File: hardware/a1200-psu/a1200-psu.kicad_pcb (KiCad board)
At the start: 2 copper layers, 147 x 76 mm, 28 parts, among them Q1 P2N60, U1 UC3844_DIP8, U2 PC817, U3 TL431D

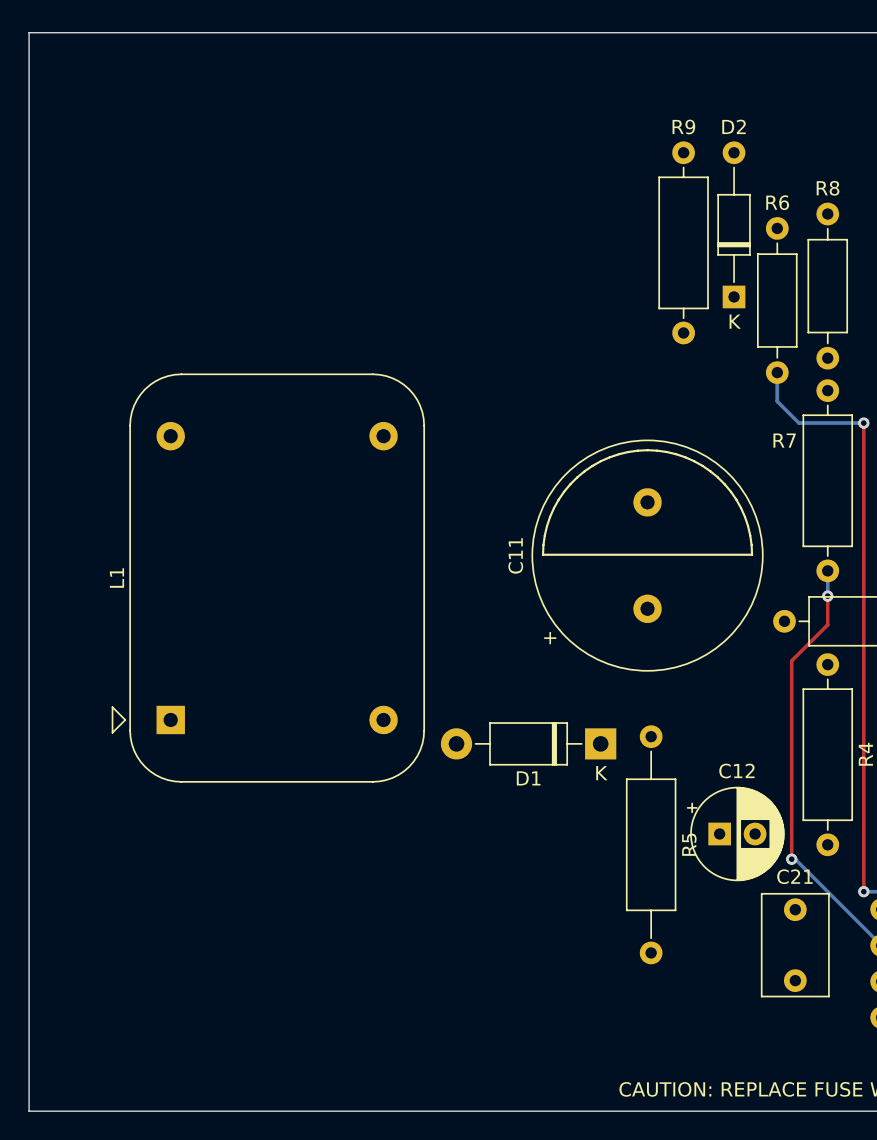
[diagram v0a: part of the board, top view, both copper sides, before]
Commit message: Add more components to PCB
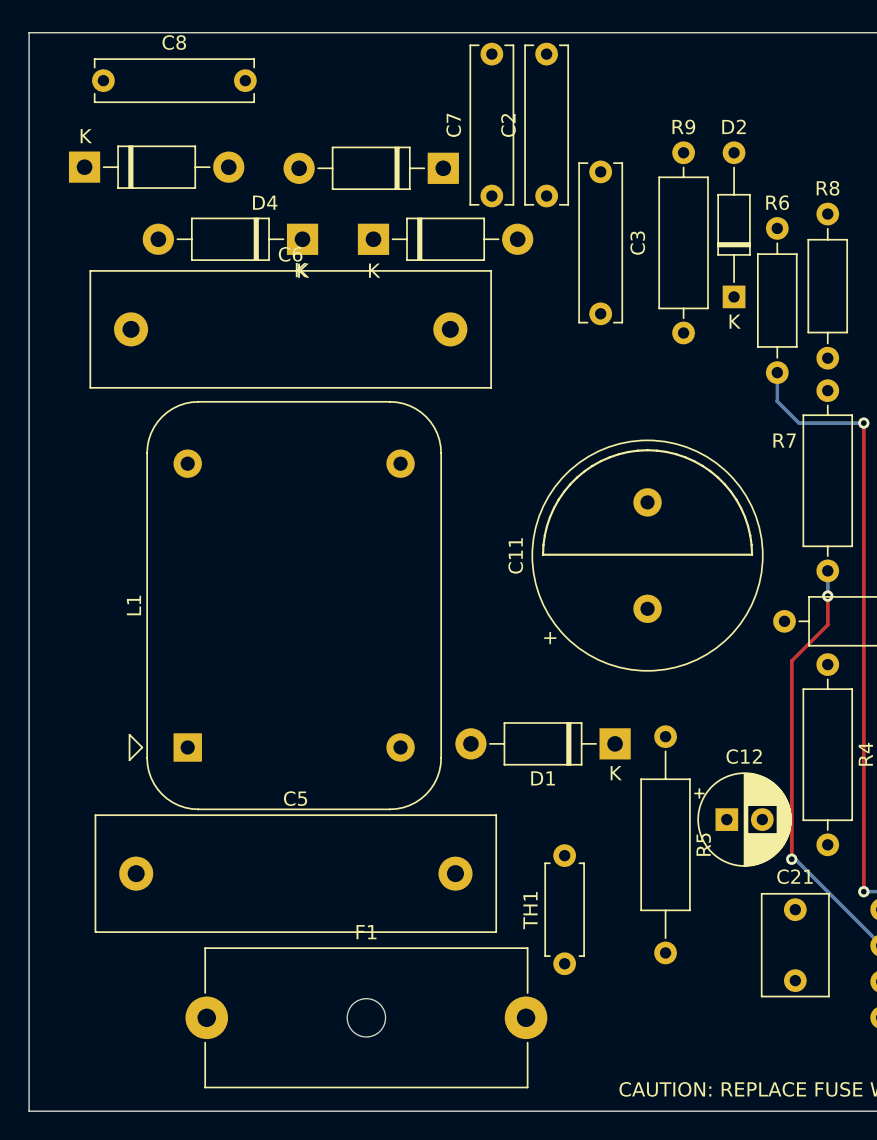
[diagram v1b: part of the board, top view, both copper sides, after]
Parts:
- added C2: 4n7, Capacitor_THT:C_Rect_L11.0mm_W2.8mm_P10.00mm_MKT, F.Cu at (109.2, 64.0)
- added C3: 4n7, Capacitor_THT:C_Rect_L11.0mm_W2.8mm_P10.00mm_MKT, F.Cu at (113.0, 62.3)
- added C5: 220nF, Capacitor_THT:C_Rect_L28.0mm_W8.0mm_P22.50mm_MKS4, F.Cu at (80.3, 111.8)
- added C6: 220nF, Capacitor_THT:C_Rect_L28.0mm_W8.0mm_P22.50mm_MKS4, F.Cu at (79.9, 73.4)
- added C7: 4n7, Capacitor_THT:C_Rect_L11.0mm_W2.8mm_P10.00mm_MKT, F.Cu at (105.4, 64.0)
- added C8: 4n7, Capacitor_THT:C_Rect_L11.0mm_W2.8mm_P10.00mm_MKT, F.Cu at (78.0, 55.9)
- added D4: 1N4007, Amiga 1200:Diode_Bridge, F.Cu at (89.4, 64.5)
- added F1: 250V T 1A, Fuse:Fuseholder_Cylinder-5x20mm_Schurter_0031_8201_Horizontal_Open, F.Cu at (85.3, 121.9)
- added TH1: 30R, Resistor_THT:R_Axial_DIN0207_L6.3mm_D2.5mm_P7.62mm_Horizontal, F.Cu at (110.5, 118.1)
- moved L1 2.28 mm to (83.9, 102.9)
- moved C12 1.14 mm to (121.9, 108.0)
- moved D1 1.02 mm to (114.0, 102.6)
- moved R5 1.02 mm to (117.6, 102.1)
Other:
- board text removed: "TODO: Change footprint to 22mm"

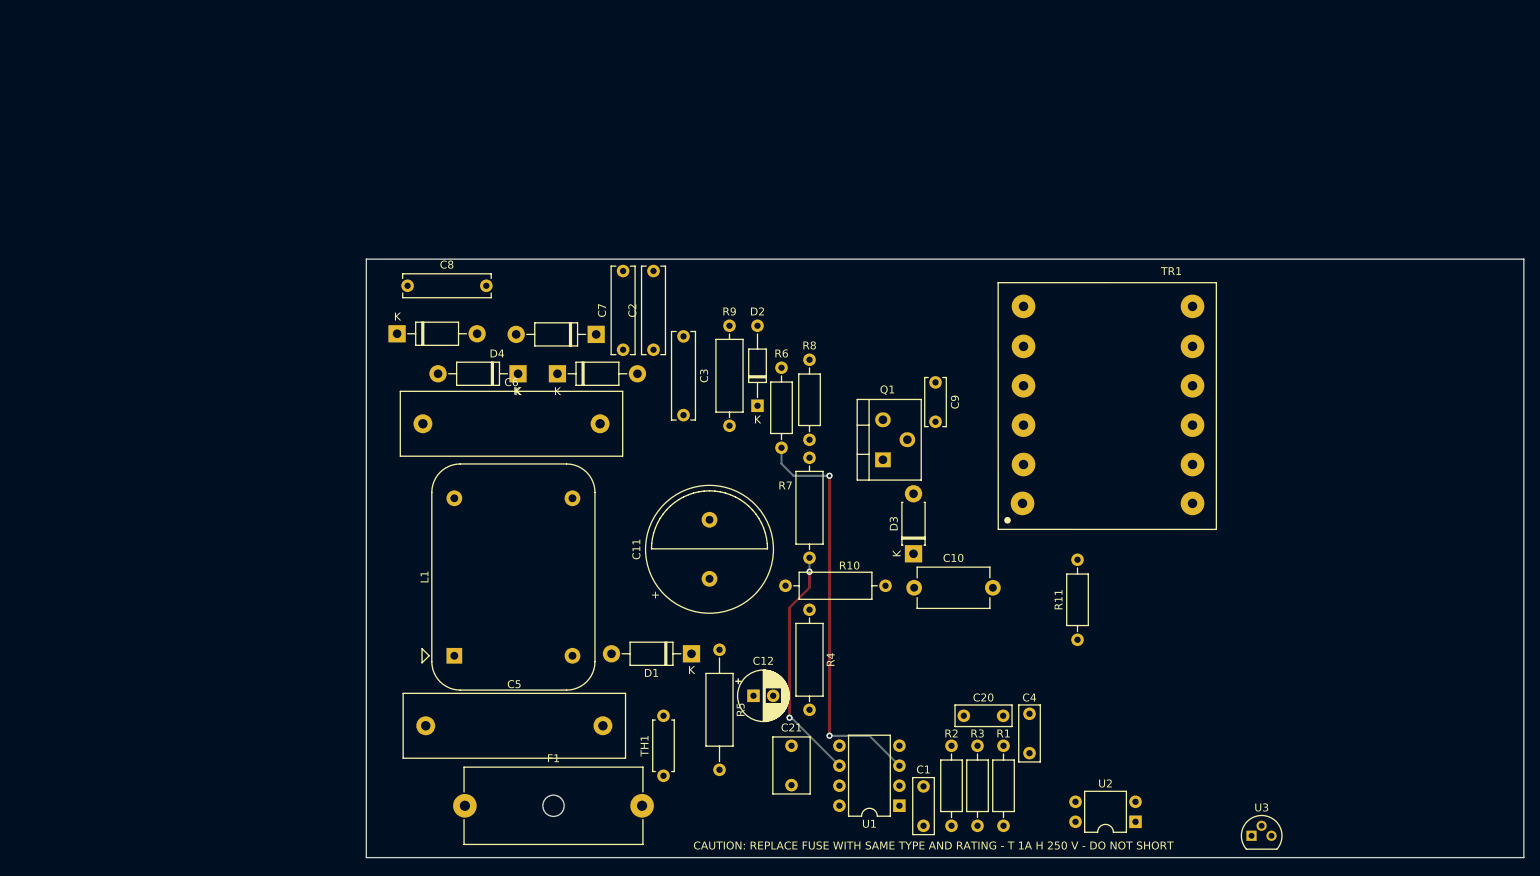
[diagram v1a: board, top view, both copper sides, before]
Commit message: Finished PCB and add missing parts
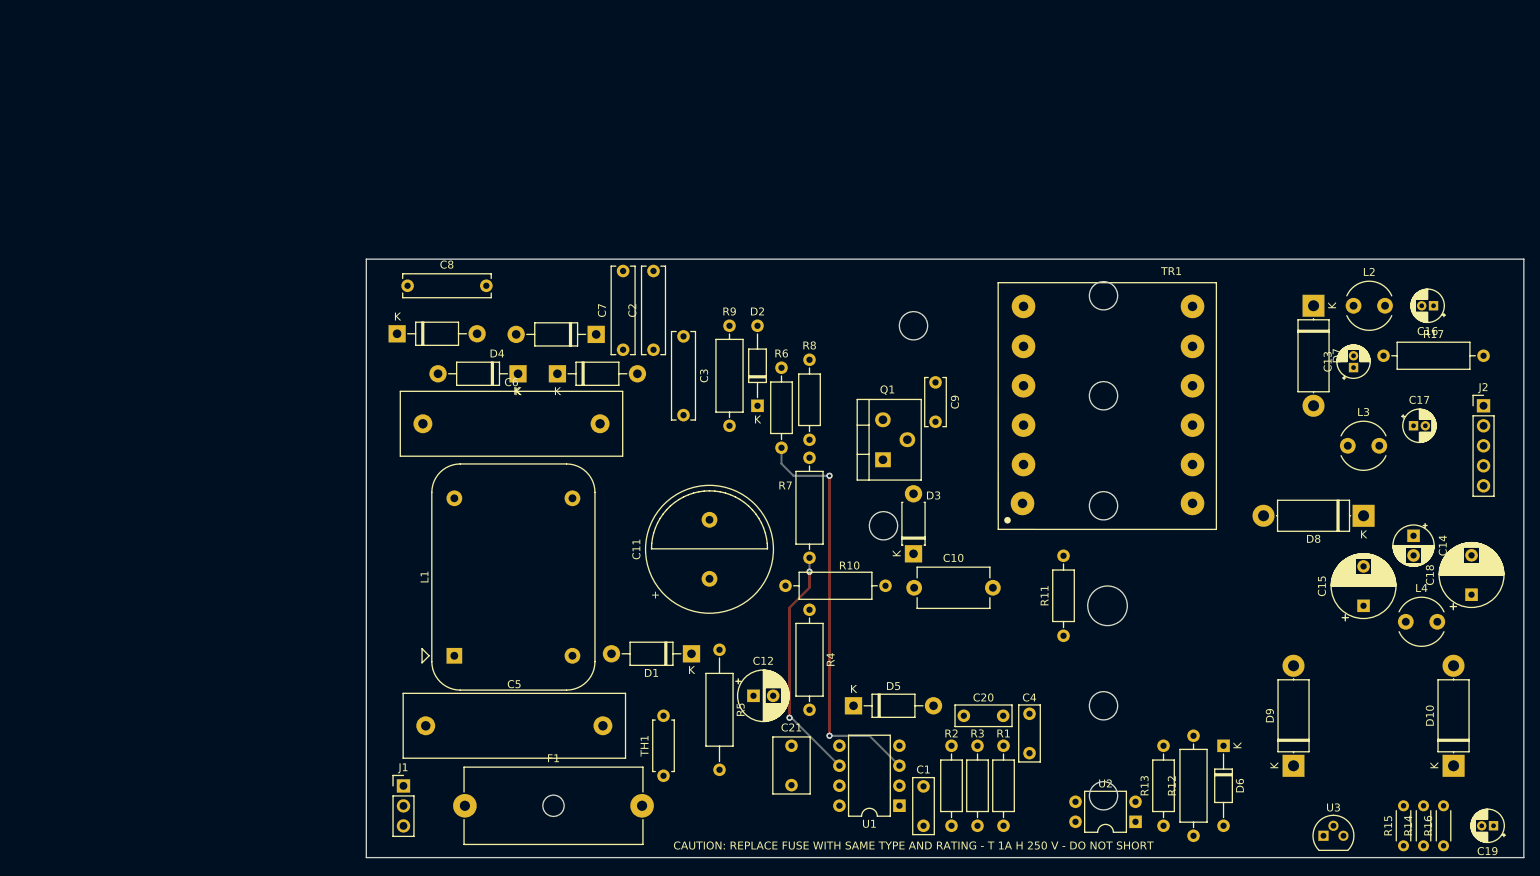
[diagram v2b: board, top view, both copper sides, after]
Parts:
- added C13: 82uF, Capacitor_THT:CP_Radial_D4.0mm_P1.50mm, F.Cu at (198.1, 66.3)
- added C14: 220uF, Capacitor_THT:CP_Radial_D5.0mm_P2.50mm, F.Cu at (205.7, 87.6)
- added C15: 1000uF, Capacitor_THT:CP_Radial_D8.0mm_P5.00mm, F.Cu at (199.4, 96.5)
- added C16: 47uF, Capacitor_THT:CP_Radial_D4.0mm_P1.50mm, F.Cu at (208.3, 58.4)
- added C17: 47uF, Capacitor_THT:CP_Radial_D4.0mm_P1.50mm, F.Cu at (205.7, 73.7)
- added C18: 1000uF, Capacitor_THT:CP_Radial_D8.0mm_P5.00mm, F.Cu at (213.1, 95.1)
- added C19: 1uF, Capacitor_THT:CP_Radial_D4.0mm_P1.50mm, F.Cu at (215.9, 124.5)
- added D10: MR852, Diode_THT:D_5W_P12.70mm_Horizontal, F.Cu at (210.8, 116.8)
- added D5: 1N4935, Diode_THT:D_DO-41_SOD81_P10.16mm_Horizontal, F.Cu at (134.6, 109.2)
- added D6: BZX55, Diode_THT:D_DO-35_SOD27_P10.16mm_Horizontal, F.Cu at (181.6, 114.3)
- added D7: 1N54xx, Diode_THT:D_5W_P12.70mm_Horizontal, F.Cu at (193.0, 58.4)
- added D8: MR852, Diode_THT:D_5W_P12.70mm_Horizontal, F.Cu at (199.4, 85.1)
- added D9: MR852, Diode_THT:D_5W_P12.70mm_Horizontal, F.Cu at (190.5, 116.8)
- added J1: 220V, Connector_PinHeader_2.54mm:PinHeader_1x03_P2.54mm_Vertical, F.Cu at (77.5, 119.4)
- added J2: Conn_01x05, Connector_PinHeader_2.54mm:PinHeader_1x05_P2.54mm_Vertical, F.Cu at (214.6, 71.1)
- added L2: L_Small, Inductor_THT:L_Radial_D6.0mm_P4.00mm, F.Cu at (198.1, 58.4)
- added L3: L_Small, Inductor_THT:L_Radial_D6.0mm_P4.00mm, F.Cu at (197.4, 76.2)
- added L4: L_Small, Inductor_THT:L_Radial_D6.0mm_P4.00mm, F.Cu at (204.8, 98.6)
- added R12: 47R, Resistor_THT:R_Axial_DIN0309_L9.0mm_D3.2mm_P12.70mm_Horizontal, F.Cu at (177.8, 125.7)
- added R13: ?, Resistor_THT:R_Axial_DIN0207_L6.3mm_D2.5mm_P10.16mm_Horizontal, F.Cu at (174.0, 124.5)
- added R14: 200k, Resistor_THT:R_Axial_DIN0204_L3.6mm_D1.6mm_P5.08mm_Horizontal, F.Cu at (207.0, 127.0)
- added R15: 33k, Resistor_THT:R_Axial_DIN0204_L3.6mm_D1.6mm_P5.08mm_Horizontal, F.Cu at (204.5, 127.0)
- added R16: 33k, Resistor_THT:R_Axial_DIN0204_L3.6mm_D1.6mm_P5.08mm_Horizontal, F.Cu at (209.6, 127.0)
- added R17: ?, Resistor_THT:R_Axial_DIN0309_L9.0mm_D3.2mm_P12.70mm_Horizontal, F.Cu at (201.9, 64.8)
- U3: footprint Package_TO_SOT_THT:TO-92L -> Package_TO_SOT_THT:TO-92
- moved U3 9.13 mm to (194.3, 125.7)
- moved R11 1.85 mm to (161.3, 100.3)
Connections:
- TR1 pad 2: (no net) -> unconnected-(TR1-Pad2)
- TR1 pad 4: (no net) -> unconnected-(TR1-Pad4)
- U3 pad 3: GND -> Net-(C19-Pad1)
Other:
- outline, holes or cut-outs redrawn

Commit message: Replace pin headers with terminals
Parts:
- J1: footprint Connector_PinHeader_2.54mm:PinHeader_1x03_P2.54mm_Vertical -> TerminalBlock_Phoenix:TerminalBlock_Phoenix_MPT-0,5-3-2.54_1x03_P2.54mm_Horizontal
- J2: footprint Connector_PinHeader_2.54mm:PinHeader_1x05_P2.54mm_Vertical -> TerminalBlock_Phoenix:TerminalBlock_Phoenix_MPT-0,5-5-2.54_1x05_P2.54mm_Horizontal
- moved J2 11.9 mm to (213.7, 83.0), turned to 90 degrees
- moved J1 0.58 mm to (78.0, 119.5), turned to -90 degrees

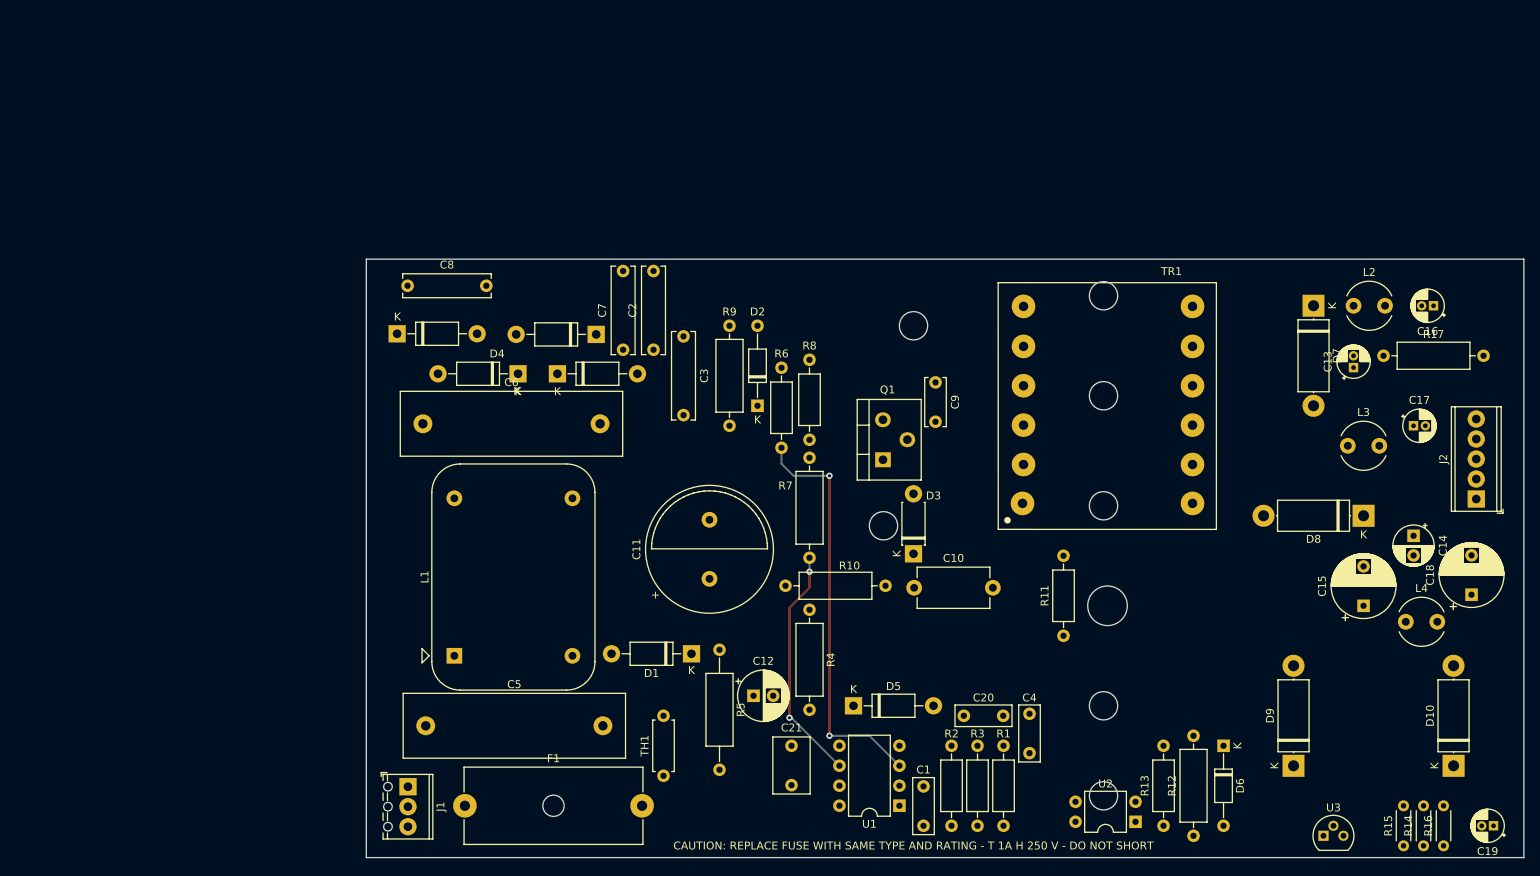
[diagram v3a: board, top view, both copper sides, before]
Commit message: Fixed various PCB layout errors
Also fixed:
- R value
- Live/PWM IC connection
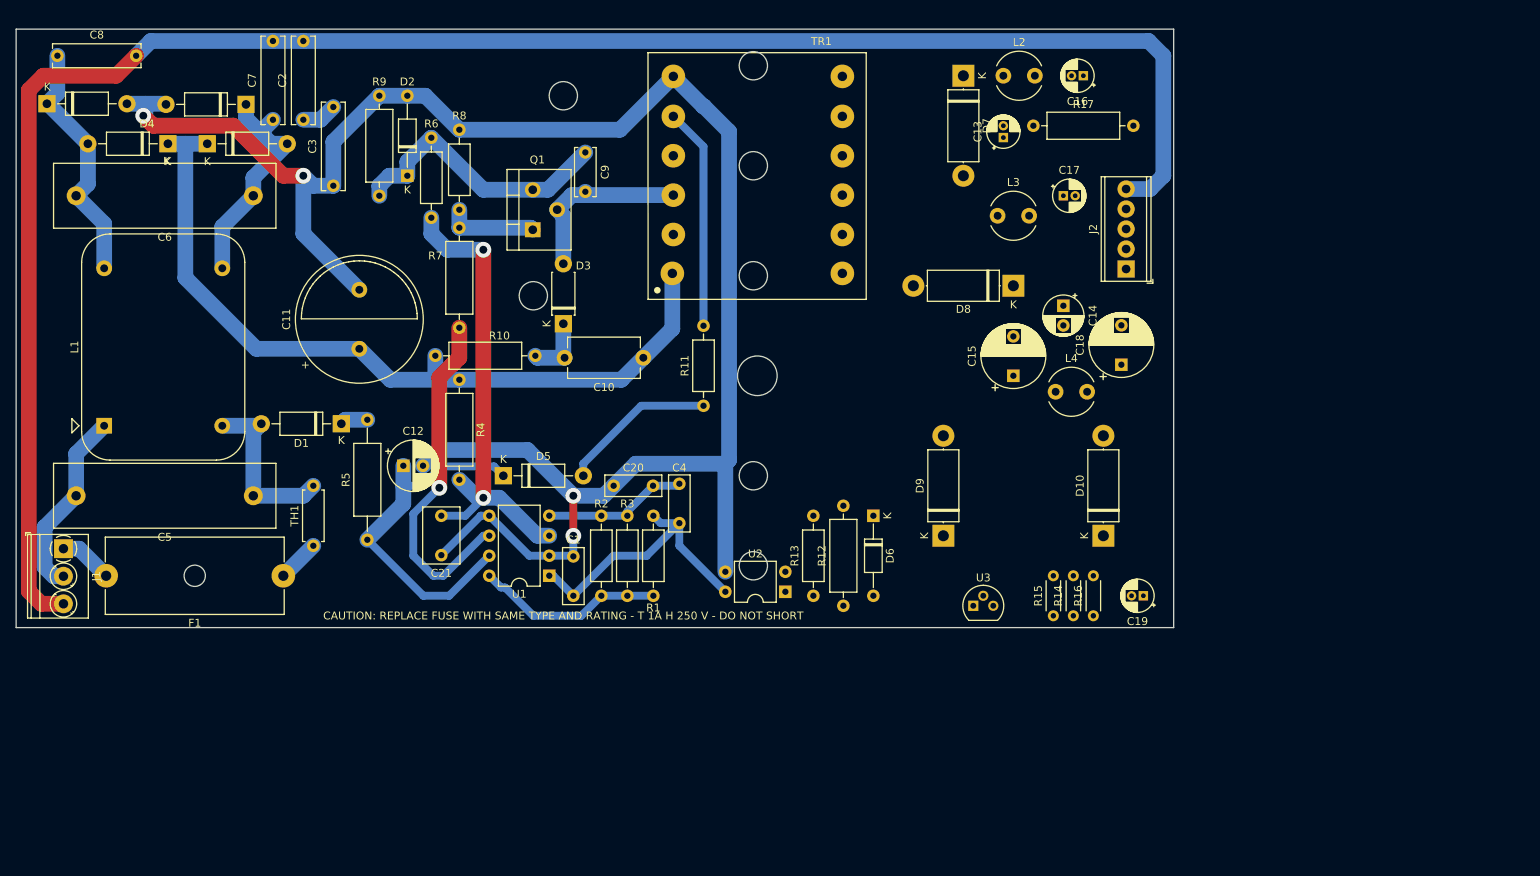
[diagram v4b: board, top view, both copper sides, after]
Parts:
- J1: footprint TerminalBlock_Phoenix:TerminalBlock_Phoenix_MPT-0,5-3-2.54_1x03_P2.54mm_Horizontal -> TerminalBlock_Phoenix:TerminalBlock_Phoenix_PT-1,5-3-3.5-H_1x03_P3.50mm_Horizontal
- R11: value 20k -> 10R
- moved C21 56.1 mm to (82.3, 85.1), turned to -90 degrees
- moved R11 54.3 mm to (115.6, 71.1)
- moved D6 53.2 mm to (137.1, 85.1)
- moved C4 53.2 mm to (112.5, 86.0)
- moved R4 53.2 mm to (84.6, 67.8)
- moved R7 53.2 mm to (84.6, 48.5)
- moved R8 53.2 mm to (84.6, 46.2)
- moved C12 53.2 mm to (77.5, 78.7)
- moved D1 53.2 mm to (69.6, 73.4)
- moved D10 53.2 mm to (166.3, 87.6)
- moved D2 53.2 mm to (78.0, 41.9)
- moved D3 53.2 mm to (97.8, 60.7)
- moved D4 53.2 mm to (44.9, 35.3)
- moved D9 53.2 mm to (146.0, 87.6)
- moved L1 53.2 mm to (39.5, 73.7)
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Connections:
- C5 pad 1: Net-(C5-Pad1) -> /Live_Pre_LF
- D1 pad 2: Net-(C5-Pad2) -> /Live_Pre_LF
- F1 pad 2: Net-(F1-Pad2) -> Net-(J1-Pad1)
- L1 pad 1: Net-(C5-Pad1) -> Net-(C5-Pad2)
- L1 pad 2: Net-(C6-Pad1) -> Net-(C6-Pad2)
- L1 pad 3: Net-(C5-Pad2) -> /Live_Pre_LF
- L1 pad 4: Net-(C6-Pad2) -> Net-(C6-Pad1)
- R5 pad 1: Net-(D1-Pad1) -> +12VA
- R5 pad 2: +12VA -> Net-(D1-Pad1)
- TH1 pad 2: Net-(C5-Pad1) -> /Live_Pre_LF
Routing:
- net GNDD: track 0.00 -> 245.8 mm, vias 0 -> 4
- net Earth: track 0.00 -> 236.8 mm
- net Net-(C10-Pad1): track 0.00 -> 102.0 mm
- net +12VA: track 0.00 -> 46.0 mm
- net Net-(C1-Pad2): track 0.00 -> 36.2 mm
- net Net-(C9-Pad1): track 0.00 -> 35.7 mm
- net Net-(C6-Pad2): track 0.00 -> 31.9 mm
- net Net-(C6-Pad1): track 0.00 -> 30.1 mm
- net Net-(R11-Pad2): track 0.00 -> 28.2 mm
- net Net-(R1-Pad1): track 0.00 -> 24.0 mm
- net Net-(C5-Pad2): track 0.00 -> 24.0 mm
- net Net-(C9-Pad2): track 0.00 -> 23.2 mm
- net /Live_Pre_LF: track 0.00 -> 22.8 mm
- net Net-(D5-Pad2): track 0.00 -> 19.9 mm
- net Net-(C20-Pad2): track 0.00 -> 18.5 mm
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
